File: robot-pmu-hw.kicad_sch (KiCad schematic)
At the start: 0 parts

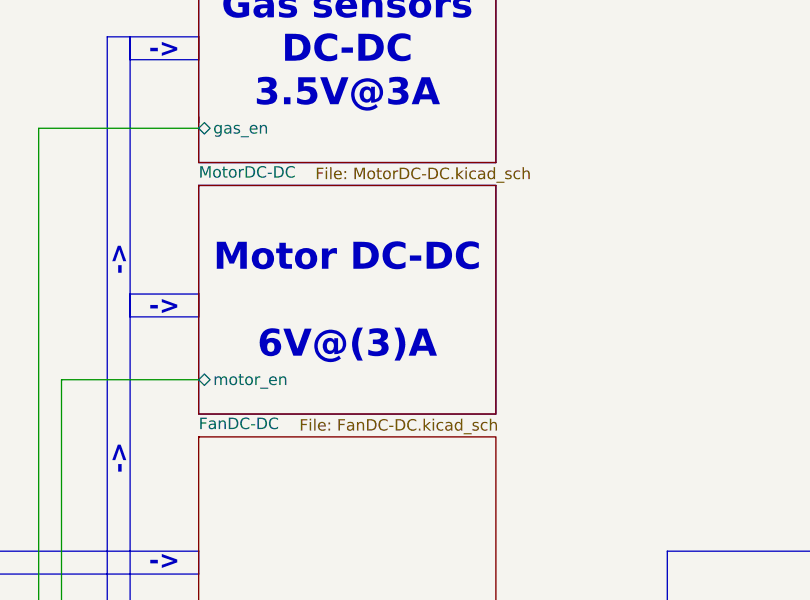
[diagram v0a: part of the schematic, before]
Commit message: Schematic fix, Example SMPS layout
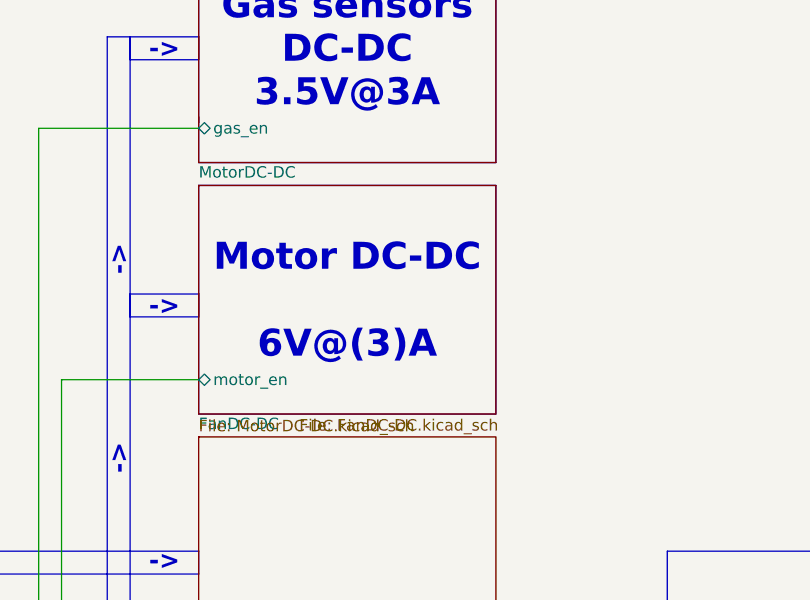
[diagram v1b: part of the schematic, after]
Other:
- sheet MotorDC-DC ports: added motor_en; removed motor_en 
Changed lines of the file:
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@@
 		(on_board yes)
 		(dnp no)
+		(fields_autoplaced yes)
 		(stroke
 			(width 0.1524)
@@
 		)
 		(property "Sheetfile" "MotorDC-DC.kicad_sch"
-			(at 280.924 93.218 0)
+			(at 267.97 121.2346 0)
 			(effects
 				(font
@@
 			)
 		)
-		(pin "motor_en " bidirectional
+		(pin "motor_en" bidirectional
 			(at 267.97 116.84 180)
 			(effects

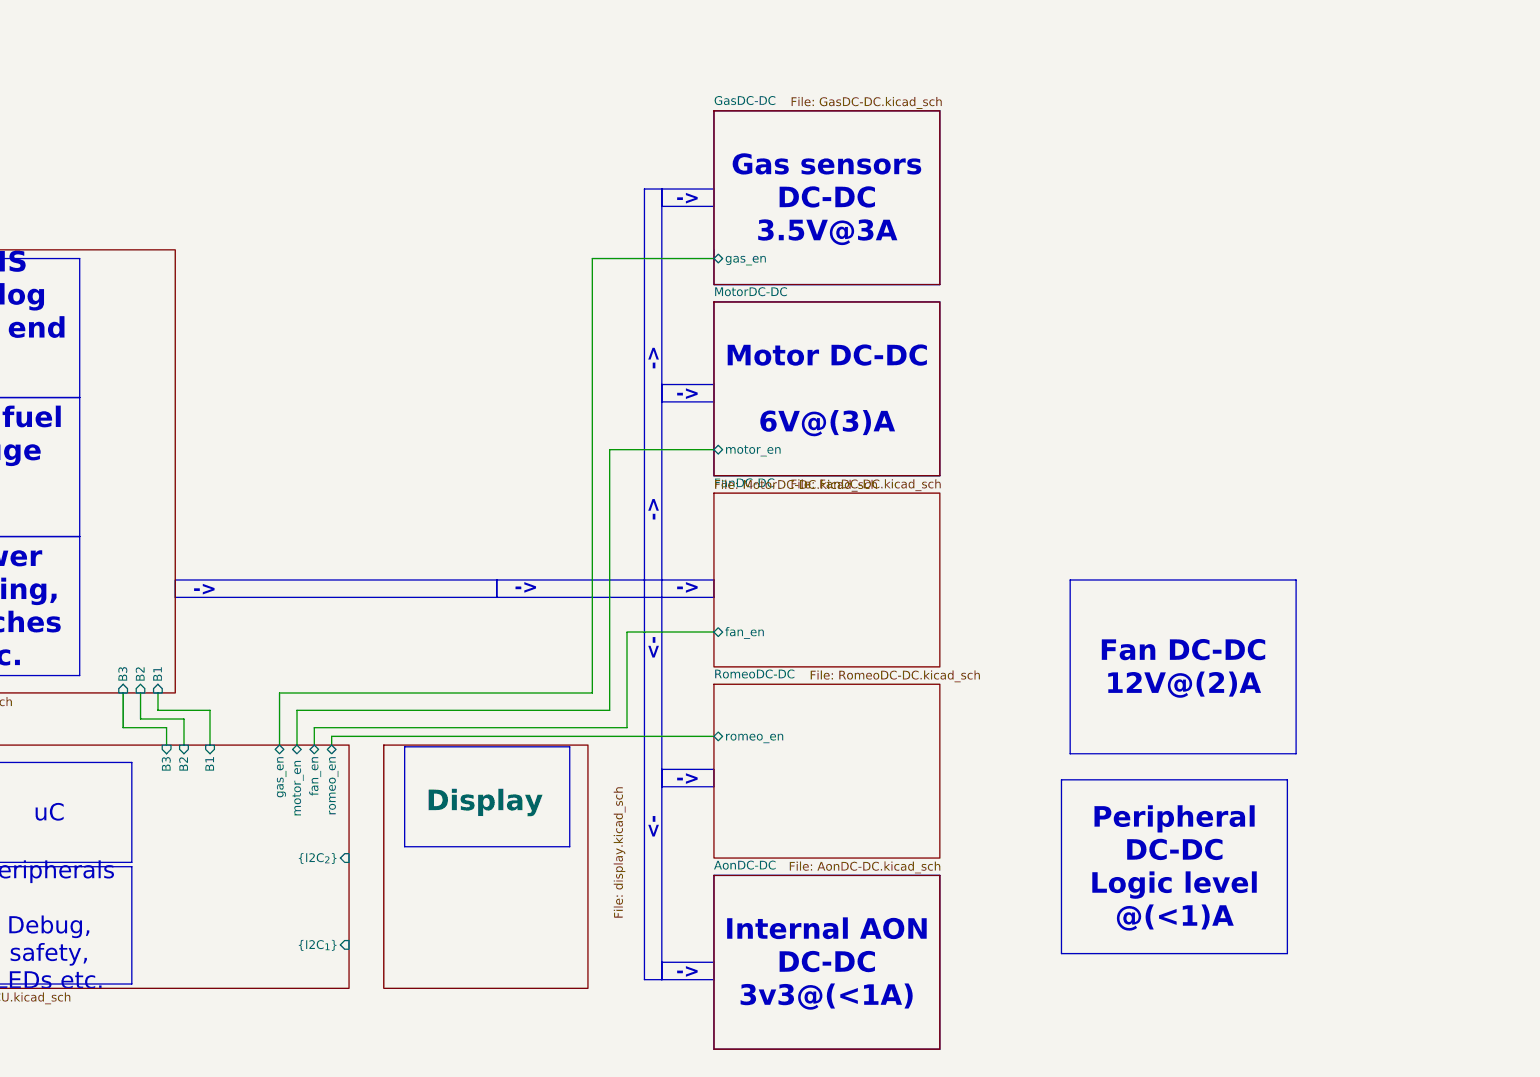
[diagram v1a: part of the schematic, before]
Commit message: Adjustable output
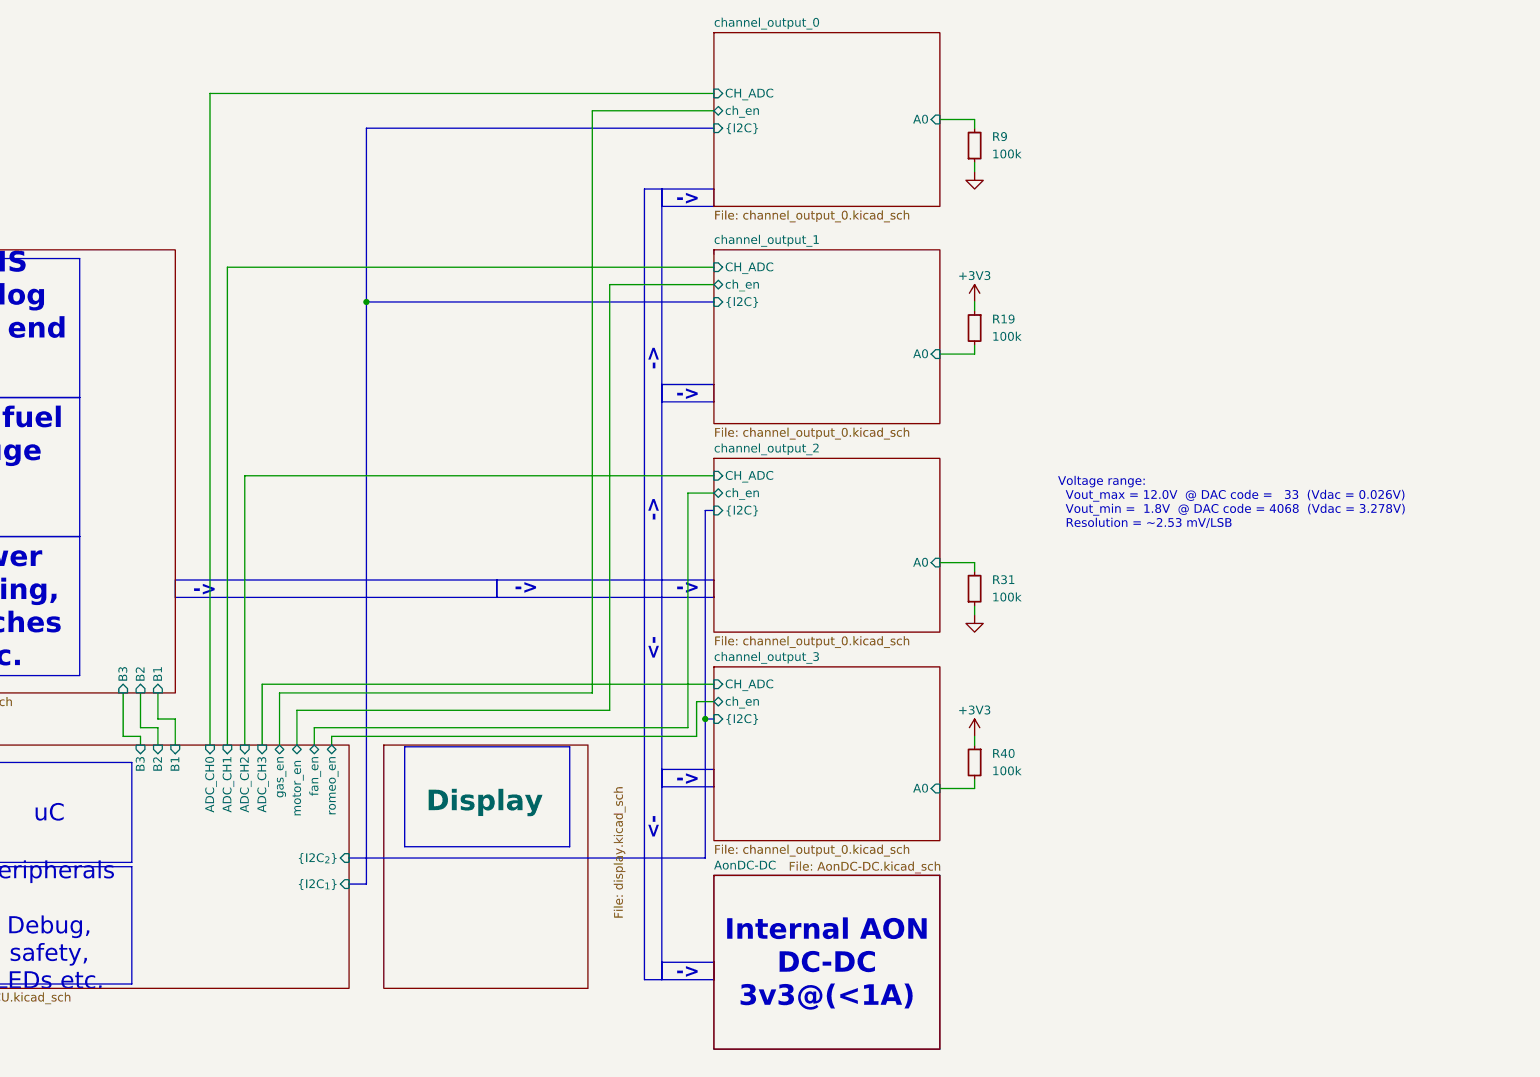
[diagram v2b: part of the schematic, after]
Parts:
- added R19, R31, R40, R9: R_100k_0402, Hardware Components Footprints:R_0402_1005Metric, symbol Hardware Components:R_100k_0402
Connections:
- new net +3V3: R19.1, R40.1
- new net GND: R31.1, R9.1
- new net channel_output_0/A0: R9.2
- new net channel_output_1/A0: R19.2
- new net channel_output_2/A0: R31.2
- new net channel_output_3/A0: R40.2
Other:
- removed sheet FanDC-DC
- removed sheet GasDC-DC
- removed sheet MotorDC-DC
- removed sheet RomeoDC-DC
- added sheet channel_output_0 (channel_output_0.kicad_sch)
- added sheet channel_output_1 (channel_output_0.kicad_sch)
- added sheet channel_output_2 (channel_output_0.kicad_sch)
- added sheet channel_output_3 (channel_output_0.kicad_sch)
- sheet uC ports: added ADC_CH0, ADC_CH1, ADC_CH2, ADC_CH3; removed none
- note added: "Voltage range: Vout_max = 12.0V @ DAC code = 33 (Vdac = 0.026V) Vout_min = 1.8V @ DAC code = 4068 (Vdac = 3.278V) Resolution = ~2.53 mV/LSB"
